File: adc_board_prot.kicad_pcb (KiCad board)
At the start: 6 copper layers, 146 x 138.7 mm, 353 parts, among them J1 USB4105-GF-A, J2 TMJG4820GENL, J3 5747841-4, J4 5747841-4, SW1 SDA02H1SBDR, SW2 FSM6JSMATR, U1 ADA4945-1, U10 LT3579, U11 LT3093, U12 LT8624S, U13 LT3045, U14 LT3045, U15 LT3045, U16 LT3045, U17 ADA4945-1, U18 LTC2387-18, U19 ADA4945-1, U2 LTC2387-18, U20 LTC2387-18, U21 ADA4945-1, U22 LTC2387-18, U23 24LC16BT-I/OT, U24 Si5342A-D, U3 93AA56BT-I/OT, U4 FT2232HL, U5 TVS1800DRV, U6 TPS259480AYWPR, U7 LT8642S, U8 LT8350S, U9 LT3042, X1 ECS-2520MVLC-120-CN-TR, Y1 CX3225SB48000D0FLJCC

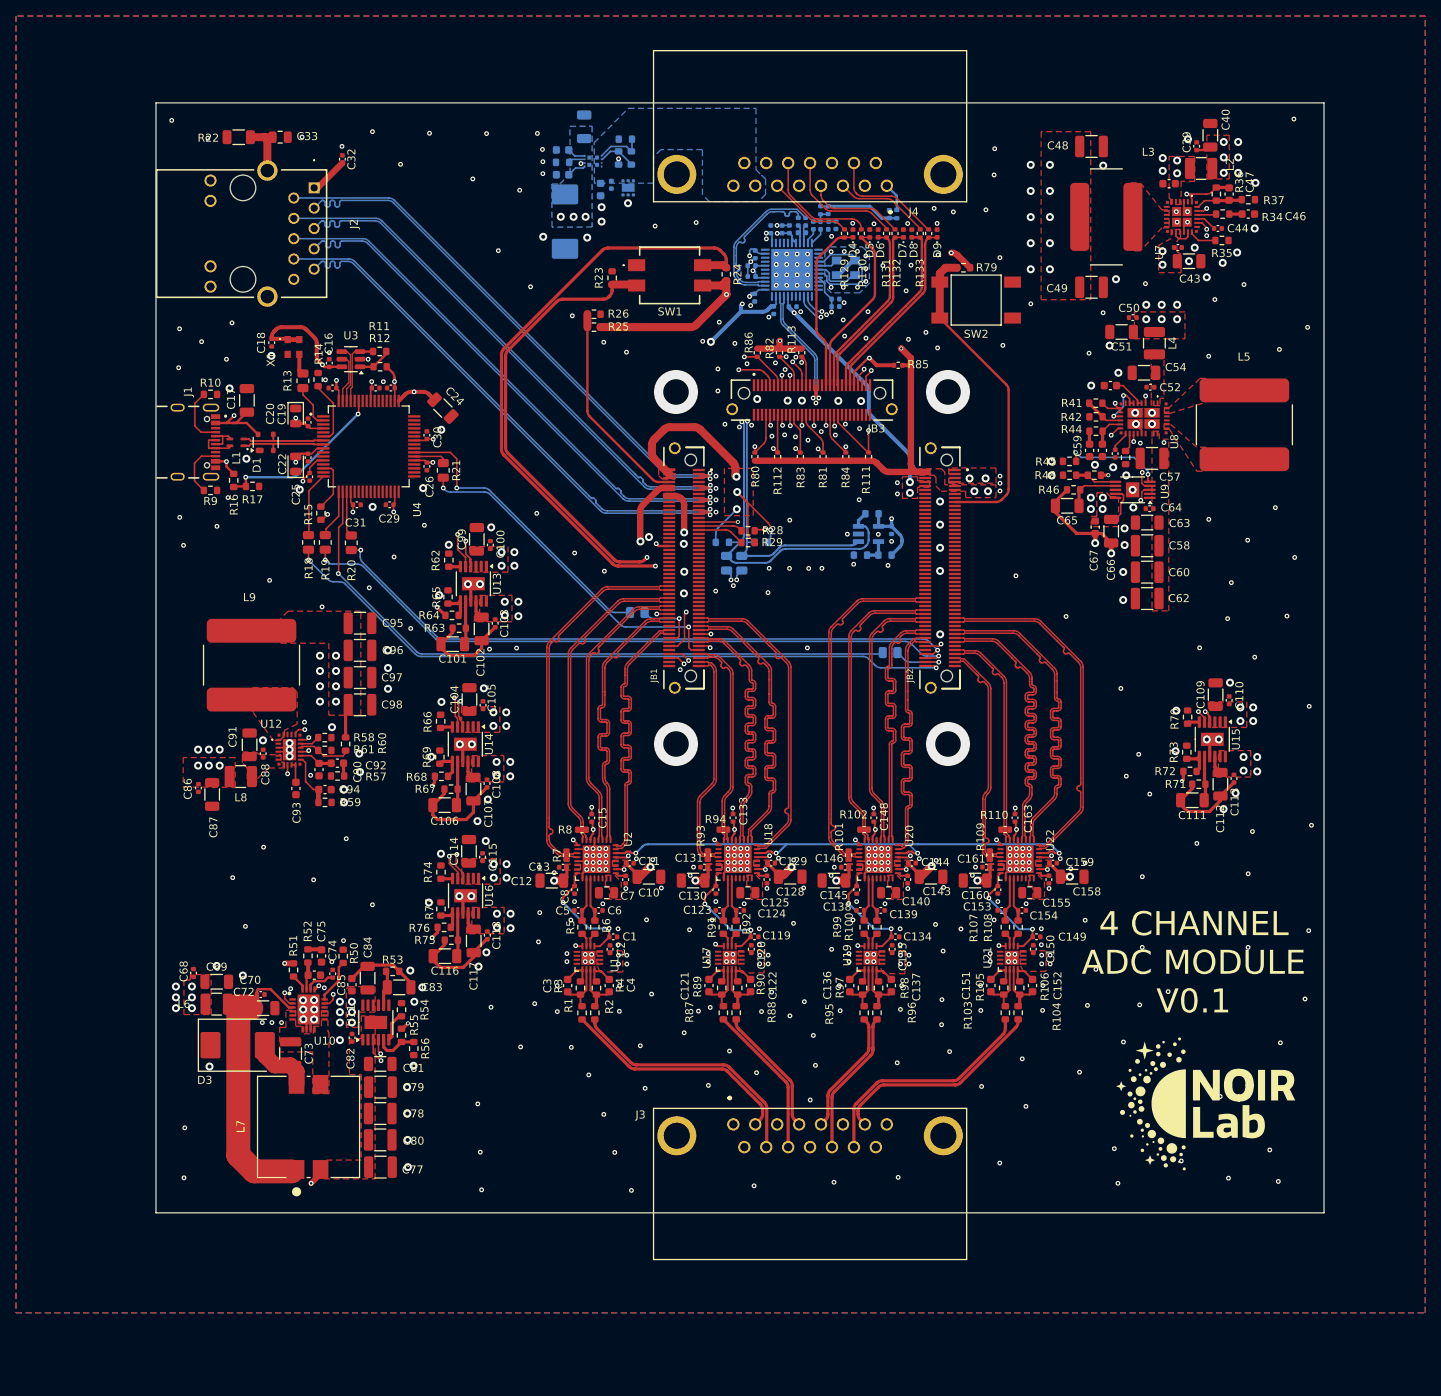
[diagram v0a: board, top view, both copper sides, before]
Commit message: add instrumentation amplifier front-end
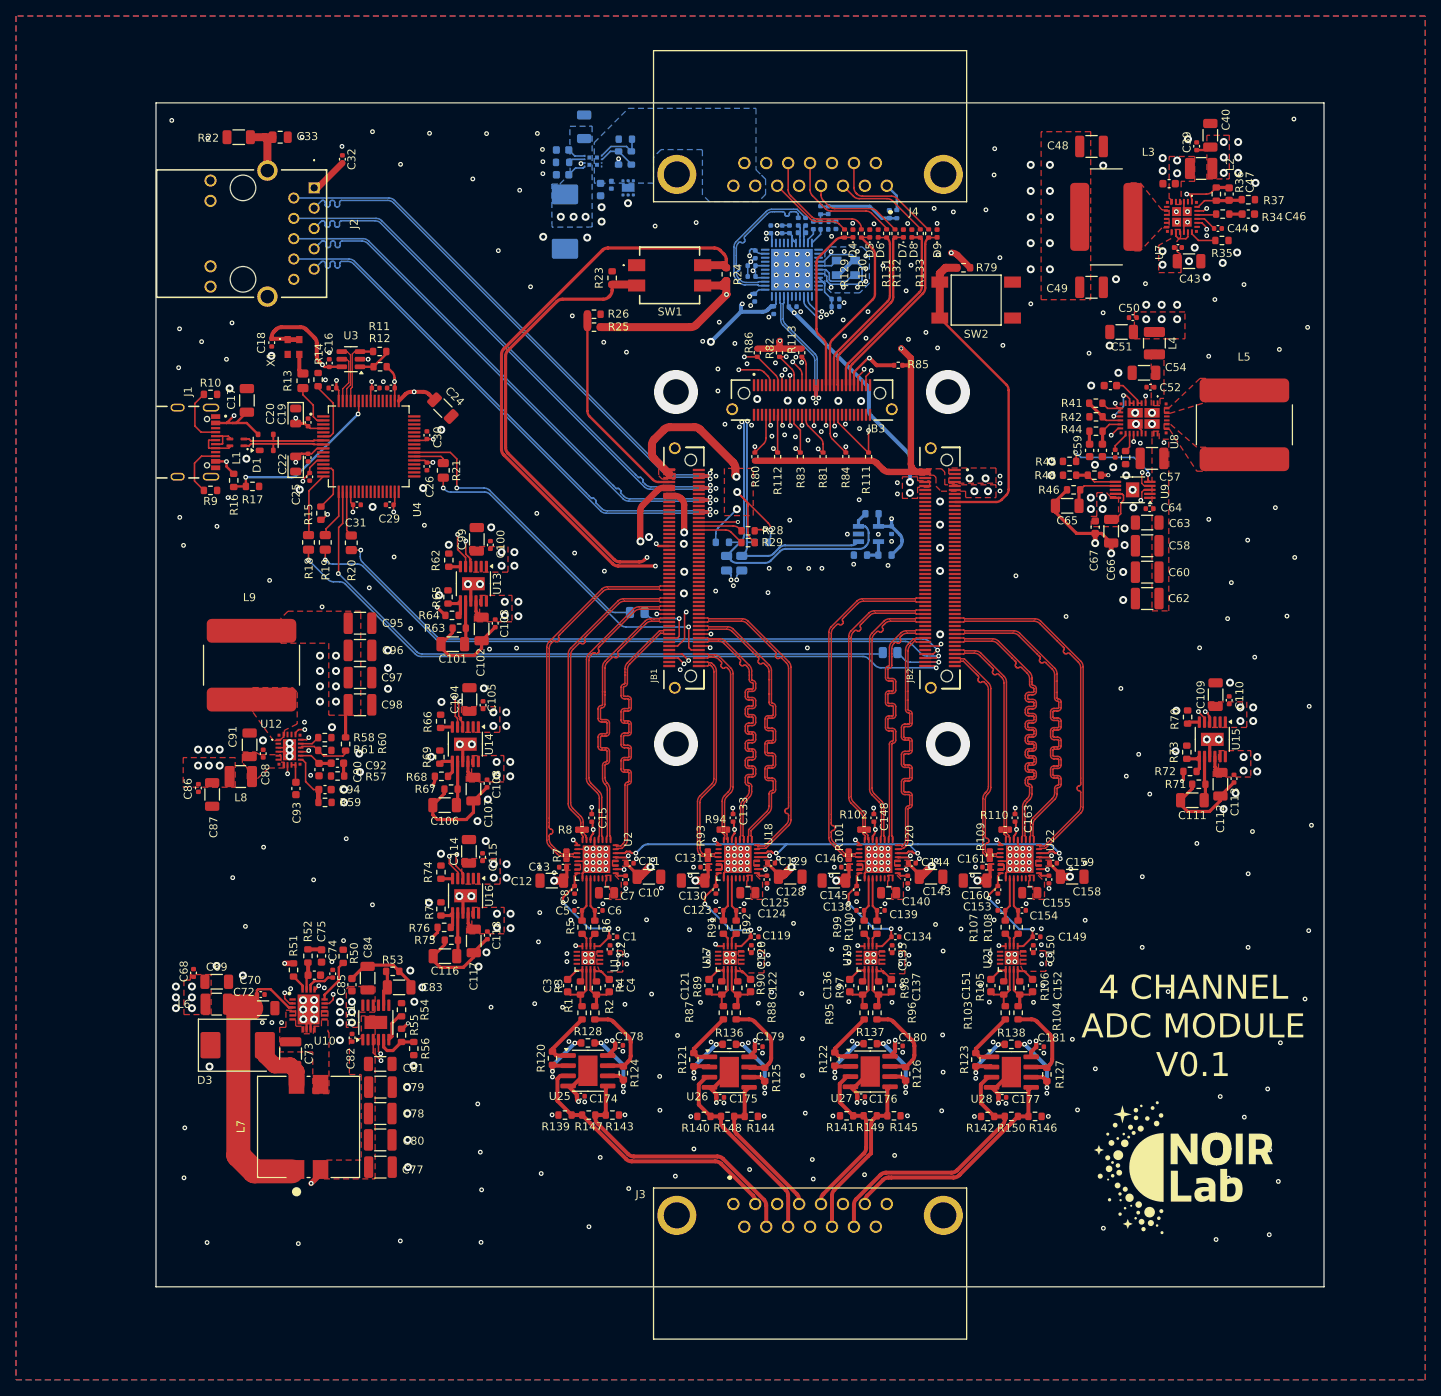
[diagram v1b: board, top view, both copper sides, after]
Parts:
- added C174: 0.1uF, Capacitor_SMD:C_0402_1005Metric, F.Cu at (123.1, 136.5)
- added C175: 0.1uF, Capacitor_SMD:C_0402_1005Metric, F.Cu at (140.5, 136.7)
- added C176: 0.1uF, Capacitor_SMD:C_0402_1005Metric, F.Cu at (158.1, 136.6)
- added C177: 0.1uF, Capacitor_SMD:C_0402_1005Metric, F.Cu at (175.8, 136.7)
- added C178: 0.1uF, Capacitor_SMD:C_0402_1005Metric, F.Cu at (127.9, 130.2)
- added C179: 0.1uF, Capacitor_SMD:C_0402_1005Metric, F.Cu at (145.3, 130.3)
- added C180: 0.1uF, Capacitor_SMD:C_0402_1005Metric, F.Cu at (162.9, 130.2)
- added C181: 0.1uF, Capacitor_SMD:C_0402_1005Metric, F.Cu at (180.5, 130.3)
- added R120: 1k, Resistor_SMD:R_0603_1608Metric, F.Cu at (119.6, 131.8)
- added R121: 1k, Resistor_SMD:R_0603_1608Metric, F.Cu at (137.2, 132.0)
- added R122: 1k, Resistor_SMD:R_0603_1608Metric, F.Cu at (154.9, 131.9)
- added R123: 1k, Resistor_SMD:R_0603_1608Metric, F.Cu at (172.5, 132.0)
- added R124: 1k, Resistor_SMD:R_0603_1608Metric, F.Cu at (128.4, 133.6)
- added R125: 1k, Resistor_SMD:R_0603_1608Metric, F.Cu at (146.1, 133.8)
- added R126: 1k, Resistor_SMD:R_0603_1608Metric, F.Cu at (163.7, 133.7)
- added R127: 1k, Resistor_SMD:R_0603_1608Metric, F.Cu at (181.4, 133.8)
- added R128: 665, Resistor_SMD:R_0603_1608Metric, F.Cu at (124.0, 129.9)
- added R136: 665, Resistor_SMD:R_0603_1608Metric, F.Cu at (141.7, 130.0)
- added R137: 665, Resistor_SMD:R_0603_1608Metric, F.Cu at (159.3, 130.0)
- added R138: 665, Resistor_SMD:R_0603_1608Metric, F.Cu at (176.9, 130.0)
- added R139: 10K, Resistor_SMD:R_0603_1608Metric, F.Cu at (121.1, 138.9)
- added R140: 10K, Resistor_SMD:R_0603_1608Metric, F.Cu at (138.5, 139.1)
- added R141: 10K, Resistor_SMD:R_0603_1608Metric, F.Cu at (156.3, 139.0)
- added R142: 10K, Resistor_SMD:R_0603_1608Metric, F.Cu at (174.0, 139.1)
- added R143: 10K, Resistor_SMD:R_0603_1608Metric, F.Cu at (127.0, 138.9)
- added R144: 10K, Resistor_SMD:R_0603_1608Metric, F.Cu at (144.4, 139.1)
- added R145: 10K, Resistor_SMD:R_0603_1608Metric, F.Cu at (162.2, 139.0)
- added R146: 10K, Resistor_SMD:R_0603_1608Metric, F.Cu at (179.9, 139.1)
- added R147: 1k, Resistor_SMD:R_0603_1608Metric, F.Cu at (124.1, 138.9)
- added R148: 1k, Resistor_SMD:R_0603_1608Metric, F.Cu at (141.4, 139.1)
- added R149: 1k, Resistor_SMD:R_0603_1608Metric, F.Cu at (159.3, 139.0)
- added R150: 1k, Resistor_SMD:R_0603_1608Metric, F.Cu at (176.9, 139.1)
- added U25: ADA4898-2, Package_SO:SOIC-8-1EP_3.9x4.9mm_P1.27mm_EP2.41x3.81mm, F.Cu at (124.0, 133.3)
- added U26: ADA4898-2, Package_SO:SOIC-8-1EP_3.9x4.9mm_P1.27mm_EP2.41x3.81mm, F.Cu at (141.7, 133.5)
- added U27: ADA4898-2, Package_SO:SOIC-8-1EP_3.9x4.9mm_P1.27mm_EP2.41x3.81mm, F.Cu at (159.3, 133.4)
- added U28: ADA4898-2, Package_SO:SOIC-8-1EP_3.9x4.9mm_P1.27mm_EP2.41x3.81mm, F.Cu at (176.9, 133.5)
- R1, R103, R104, R2, R87, R88, R95, R96: value 249 -> 1k
- moved J3 9.95 mm to (142.2, 150.0)
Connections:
- R1 pad 1: IN0- -> /converters/adc_0/inst_out-
- R103 pad 1: IN3- -> /converters/adc_3/inst_out-
- R104 pad 1: IN3+ -> /converters/adc_3/inst_out+
- R2 pad 1: IN0+ -> /converters/adc_0/inst_out+
- R87 pad 1: IN1- -> /converters/adc_1/inst_out-
- R88 pad 1: IN1+ -> /converters/adc_1/inst_out+
- R95 pad 1: IN2- -> /converters/adc_2/inst_out-
- R96 pad 1: IN2+ -> /converters/adc_2/inst_out+
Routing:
- net +15VA: track 139.9 -> 243.7 mm, vias 3 -> 7
- net -15VA: track 68.1 -> 170.8 mm, vias 4 -> 8
- net /converters/adc_2/inst_out+: track 0.00 -> 11.3 mm
- net /converters/adc_1/inst_out+: track 0.00 -> 11.2 mm
- net /converters/adc_3/inst_out+: track 0.00 -> 11.2 mm
- net /converters/adc_0/inst_out+: track 0.00 -> 11.2 mm
- net /converters/adc_3/fb-: track 0.00 -> 10.4 mm, vias 0 -> 2
- net /converters/adc_2/fb-: track 0.00 -> 10.4 mm, vias 0 -> 2
- net /converters/adc_0/fb-: track 0.00 -> 10.3 mm, vias 0 -> 2
- net /converters/adc_1/fb-: track 0.00 -> 10.3 mm, vias 0 -> 2
- net /converters/adc_2/fb+: track 0.00 -> 8.31 mm, vias 0 -> 2
- net /converters/adc_3/fb+: track 0.00 -> 8.30 mm, vias 0 -> 2
- net /converters/adc_0/fb+: track 0.00 -> 8.30 mm, vias 0 -> 2
- net /converters/adc_1/fb+: track 0.00 -> 8.26 mm, vias 0 -> 2
- net /converters/adc_3/inst_out-: track 0.00 -> 7.90 mm
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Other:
- board size 146 x 138.7 mm -> 146 x 148 mm
